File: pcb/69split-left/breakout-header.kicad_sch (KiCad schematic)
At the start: 1 part, among them J4 Conn_01x09_Socket

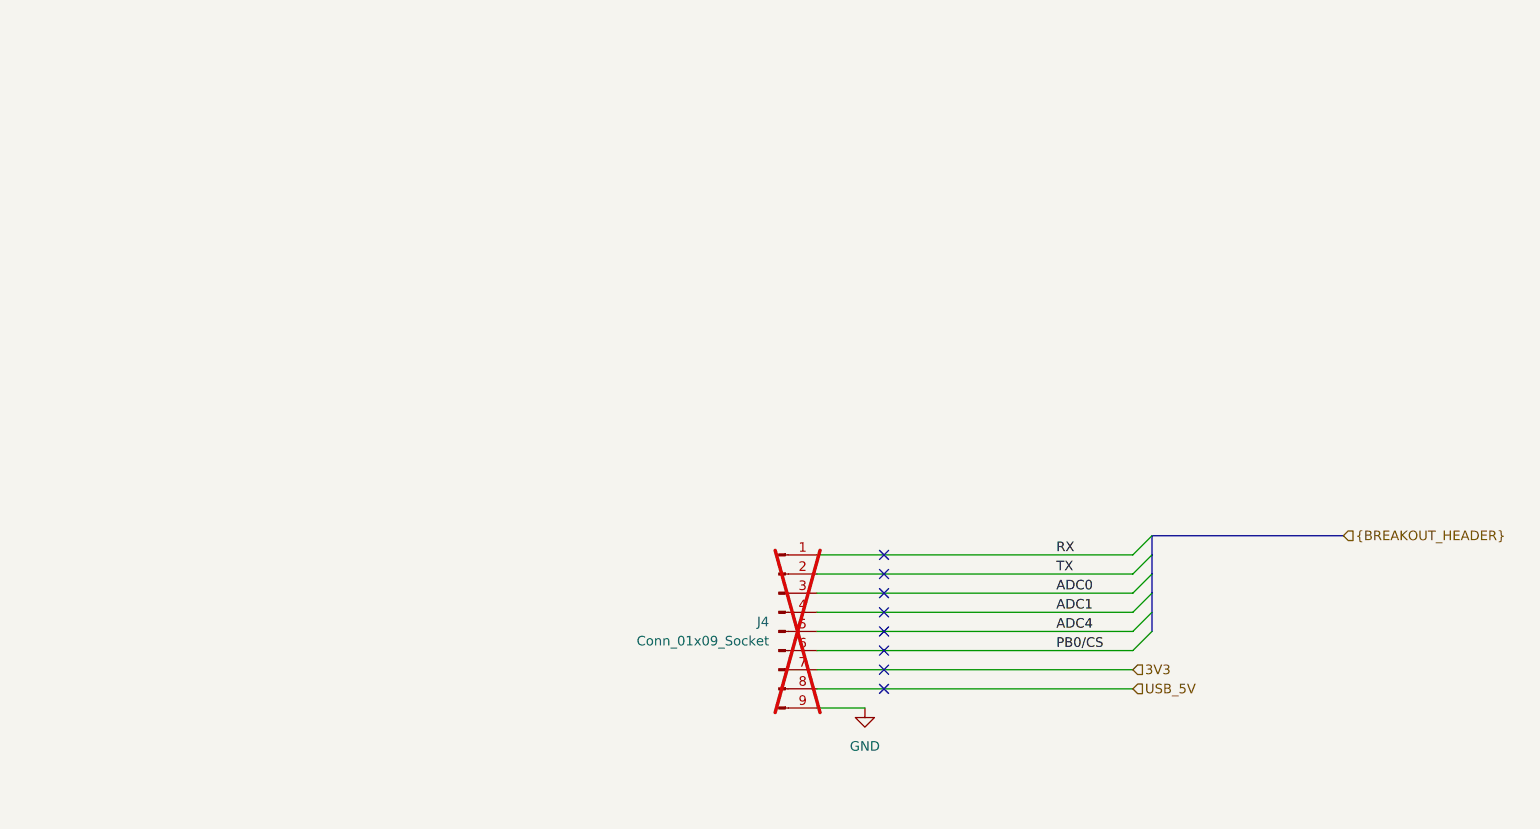
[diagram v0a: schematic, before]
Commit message: Minor improvements to left schematic and layout.
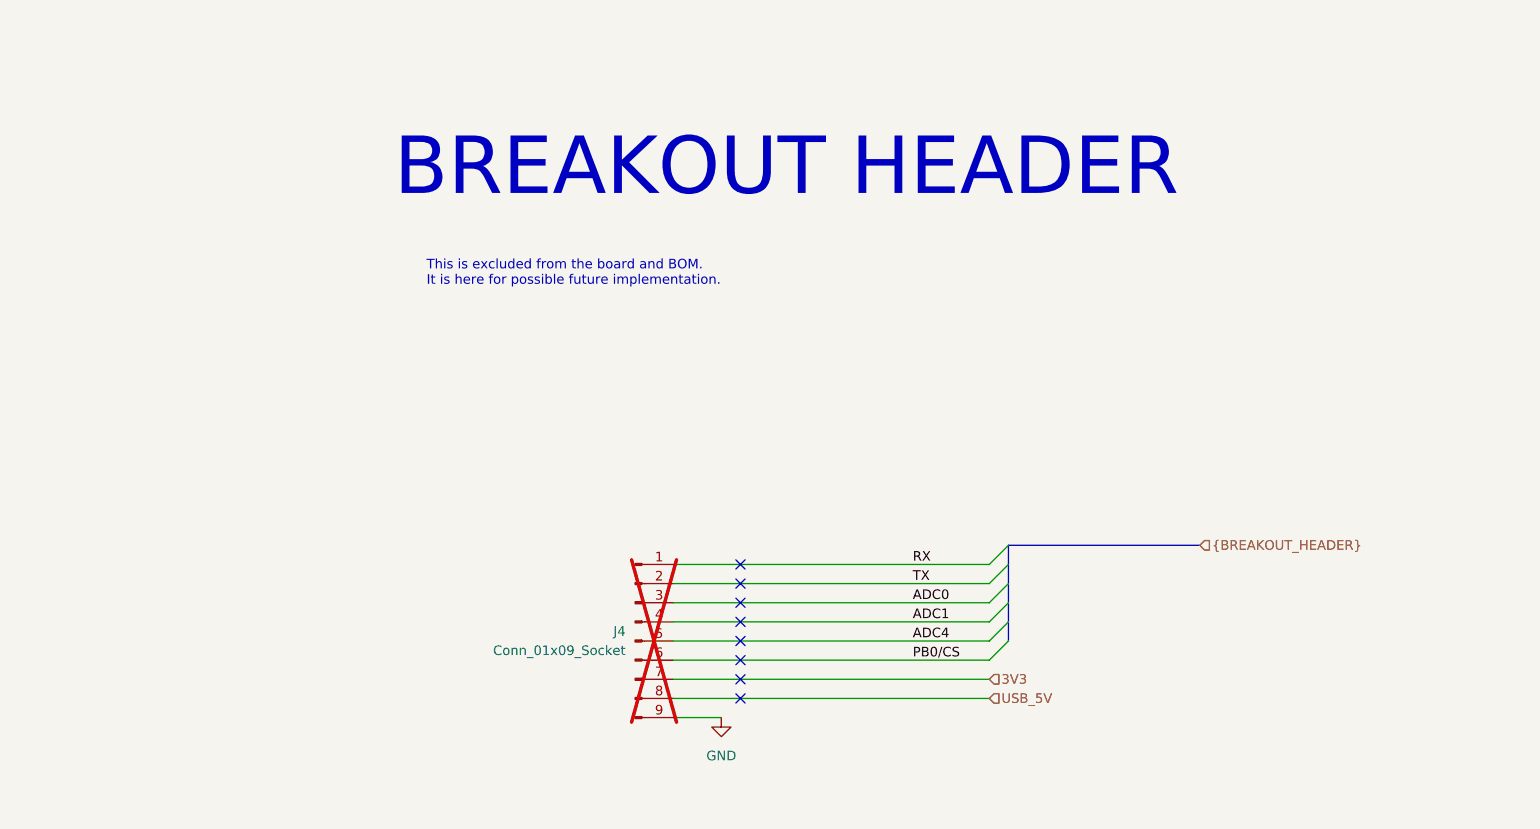
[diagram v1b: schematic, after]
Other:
- note added: "BREAKOUT HEADER"
- note added: "This is excluded from the board and BOM. It is here for possible future implementation."
- moved on the sheet: J4

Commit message: Alright I think now the left side is actually ready.
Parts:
- J4: footprint Connector_PinHeader_2.54mm:PinHeader_1x09_P2.54mm_Vertical -> Connector_PinHeader_2.54mm:PinHeader_1x11_P2.54mm_Vertical; symbol Connector:Conn_01x09_Pin -> Connector:Conn_01x11_Pin; now in the parts list
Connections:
- net 3V3: now also J4.2 (Pin_2); no longer J4.7 (Pin_7)
- net ADC0: now also J4.5 (Pin_5); no longer J4.3 (Pin_3)
- net ADC1: now also J4.6 (Pin_6); no longer J4.4 (Pin_4)
- net ADC4: now also J4.7 (Pin_7); no longer J4.5 (Pin_5)
- net GND: now also J4.11 (Pin_11); no longer J4.9 (Pin_9)
- net PB0/CS: now also J4.8 (Pin_8); no longer J4.6 (Pin_6)
- net RX: now also J4.4 (Pin_4); no longer J4.1 (Pin_1)
- net TX: now also J4.3 (Pin_3); no longer J4.2 (Pin_2)
- net USB_5V: now also J4.1 (Pin_1); no longer J4.8 (Pin_8)
- new net SCL: J4.10 (Pin_10)
- new net SDA: J4.9 (Pin_9)
- no-connect marks 8 -> 0

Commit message: Added ESD protection and better routing for the USB data lines.
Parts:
- J4: MPN (none) -> Generic
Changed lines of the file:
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@@
 			)
 		)
-		(property "MPN" ""
+		(property "MPN" "Generic"
 			(at 128.27 107.95 0)
 			(effects

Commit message: Final touches.
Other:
- note removed: "This is excluded from the board and BOM. It is here for possible future implementation."
- moved on the sheet: J4
